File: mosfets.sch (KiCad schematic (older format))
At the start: 28 parts, among them Q11 PSMN1R2-30YLC,115, Q12 PSMN1R2-30YLC,115, Q13 PSMN1R2-30YLC,115, Q14 PMPB20EN, Q15 PMPB20EN, Q16 PMPB20EN, Q17 PMPB20EN

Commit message: Current snapshot
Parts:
- renumbered R41 to R38, R42 to R39, R43 to R40, R44 to R41, R45 to R42, R46 to R43, R47 to R44, R48 to R45, R49 to R46, R50 to R47, R51 to R48, R52 to R49, R53 to R50, R54 to R51
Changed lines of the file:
@@
 $Descr A4 11693 8268
 encoding utf-8
-Sheet 7 7
+Sheet 7 11
 Title "MOSFET"
 Date ""
@@
 Comment4 ""
 $EndDescr
-Text HLabel 2600 1300 2    50   Output ~ 0
-BED_OUT
-Text HLabel 1700 1300 0    50   Output ~ 0
-VDD_BED
 $Comp
 L Device:D_Schottky D22
@@
 PWM_HEAT1
 $Comp
-L Device:R R41
+L Device:R R38
 U 1 1 5B1AEA5D
 P 1500 1750
-F 0 "R41" V 1293 1750 50  0000 C CNN
+F 0 "R38" V 1293 1750 50  0000 C CNN
 F 1 "100" V 1384 1750 50  0000 C CNN
 F 2 "Resistor_SMD:R_0603_1608Metric" V 1430 1750 50  0001 C CNN
@@
 Wire Wire Line
 	2300 1550 2300 1300
-Text HLabel 2600 2950 2    50   Output ~ 0
-HEAT1_OUT
-Text HLabel 1700 2950 0    50   Output ~ 0
-VDD_HEAT1
 $Comp
 L Device:D_Schottky D23
@@
 	2300 3850 2300 3700
 $Comp
-L Device:R R42
+L Device:R R39
 U 1 1 5B1B03DE
 P 1500 3400
-F 0 "R42" V 1293 3400 50  0000 C CNN
+F 0 "R39" V 1293 3400 50  0000 C CNN
 F 1 "100" V 1384 3400 50  0000 C CNN
 F 2 "Resistor_SMD:R_0603_1608Metric" V 1430 3400 50  0001 C CNN
@@
 $EndComp
 $Comp
-L Device:R R47
+L Device:R R44
 U 1 1 5B1FB287
 P 5150 1750
-F 0 "R47" V 4943 1750 50  0000 C CNN
+F 0 "R44" V 4943 1750 50  0000 C CNN
 F 1 "100" V 5034 1750 50  0000 C CNN
 F 2 "Resistor_SMD:R_0603_1608Metric" V 5080 1750 50  0001 C CNN
@@
 Wire Wire Line
 	4900 1750 5000 1750
-Text HLabel 6150 1300 2    50   Output ~ 0
-FAN1_OUT
 Wire Wire Line
 	5250 1300 5350 1300
@@
 	5850 1950 5850 2200
 $Comp
-L Device:R R48
+L Device:R R45
 U 1 1 5B2008D0
 P 5150 3400
-F 0 "R48" V 4943 3400 50  0000 C CNN
+F 0 "R45" V 4943 3400 50  0000 C CNN
 F 1 "100" V 5034 3400 50  0000 C CNN
 F 2 "Resistor_SMD:R_0603_1608Metric" V 5080 3400 50  0001 C CNN
@@
 Wire Wire Line
 	4900 3400 5000 3400
-Text HLabel 6150 2950 2    50   Output ~ 0
-FAN3_OUT
 Wire Wire Line
 	5250 2950 5350 2950
@@
 	1650 3400 1800 3400
 $Comp
-L Device:R R44
+L Device:R R41
 U 1 1 5AF82135
 P 1950 2200
-F 0 "R44" V 1743 2200 50  0000 C CNN
+F 0 "R41" V 1743 2200 50  0000 C CNN
 F 1 "100k" V 1834 2200 50  0000 C CNN
 F 2 "Resistor_SMD:R_0603_1608Metric" V 1880 2200 50  0001 C CNN
@@
 	1800 1750 2000 1750
 $Comp
-L Device:R R45
+L Device:R R42
 U 1 1 5AF8339E
 P 1950 3850
-F 0 "R45" V 1743 3850 50  0000 C CNN
+F 0 "R42" V 1743 3850 50  0000 C CNN
 F 1 "100k" V 1834 3850 50  0000 C CNN
 F 2 "Resistor_SMD:R_0603_1608Metric" V 1880 3850 50  0001 C CNN
@@
 	2300 3850 2100 3850
 $Comp
-L Device:R R49
+L Device:R R46
 U 1 1 5AF83BB4
 P 5600 2200
-F 0 "R49" V 5393 2200 50  0000 C CNN
+F 0 "R46" V 5393 2200 50  0000 C CNN
 F 1 "100k" V 5484 2200 50  0000 C CNN
 F 2 "Resistor_SMD:R_0603_1608Metric" V 5530 2200 50  0001 C CNN
@@
 Connection ~ 5350 1750
 $Comp
-L Device:R R50
+L Device:R R47
 U 1 1 5AF880C0
 P 5650 3850
-F 0 "R50" V 5443 3850 50  0000 C CNN
+F 0 "R47" V 5443 3850 50  0000 C CNN
 F 1 "100k" V 5534 3850 50  0000 C CNN
 F 2 "Resistor_SMD:R_0603_1608Metric" V 5580 3850 50  0001 C CNN
@@
 Text HLabel 1250 4900 0    50   Input ~ 0
 PWM_HEAT2
-Text HLabel 2600 4450 2    50   Output ~ 0
-HEAT2_OUT
-Text HLabel 1700 4450 0    50   Output ~ 0
-VDD_HEAT2
 $Comp
 L Device:D_Schottky D24
@@
 	2300 5350 2300 5200
 $Comp
-L Device:R R43
+L Device:R R40
 U 1 1 5BC4CDF3
 P 1500 4900
-F 0 "R43" V 1293 4900 50  0000 C CNN
+F 0 "R40" V 1293 4900 50  0000 C CNN
 F 1 "100" V 1384 4900 50  0000 C CNN
 F 2 "Resistor_SMD:R_0603_1608Metric" V 1430 4900 50  0001 C CNN
@@
 	1650 4900 1800 4900
 $Comp
-L Device:R R46
+L Device:R R43
 U 1 1 5BC4CE00
 P 1950 5350
-F 0 "R46" V 1743 5350 50  0000 C CNN
+F 0 "R43" V 1743 5350 50  0000 C CNN
 F 1 "100k" V 1834 5350 50  0000 C CNN
 F 2 "Resistor_SMD:R_0603_1608Metric" V 1880 5350 50  0001 C CNN
@@
 Connection ~ 2300 5350
 $Comp
-L power:GND #PWR072
+L power:GND #PWR073
 U 1 1 5BC4EE15
 P 2300 2200
-F 0 "#PWR072" H 2300 1950 50  0001 C CNN
+F 0 "#PWR073" H 2300 1950 50  0001 C CNN
 F 1 "GND" H 2305 2027 50  0000 C CNN
 F 2 "" H 2300 2200 50  0001 C CNN
@@
 $EndComp
 $Comp
-L power:GND #PWR073
+L power:GND #PWR074
 U 1 1 5BC4EE68
 P 2300 3850
-F 0 "#PWR073" H 2300 3600 50  0001 C CNN
+F 0 "#PWR074" H 2300 3600 50  0001 C CNN
 F 1 "GND" H 2305 3677 50  0000 C CNN
 F 2 "" H 2300 3850 50  0001 C CNN
@@
 $EndComp
 $Comp
-L power:GND #PWR074
+L power:GND #PWR075
 U 1 1 5BC50D60
 P 2300 5350
-F 0 "#PWR074" H 2300 5100 50  0001 C CNN
+F 0 "#PWR075" H 2300 5100 50  0001 C CNN
 F 1 "GND" H 2305 5177 50  0000 C CNN
 F 2 "" H 2300 5350 50  0001 C CNN
@@
 $EndComp
 $Comp
-L power:GND #PWR076
+L power:GND #PWR077
 U 1 1 5BC52C58
 P 5850 3850
-F 0 "#PWR076" H 5850 3600 50  0001 C CNN
+F 0 "#PWR077" H 5850 3600 50  0001 C CNN
 F 1 "GND" H 5855 3677 50  0000 C CNN
 F 2 "" H 5850 3850 50  0001 C CNN
@@
 $EndComp
 $Comp
-L power:GND #PWR075
+L power:GND #PWR076
 U 1 1 5BC54B50
 P 5850 2200
-F 0 "#PWR075" H 5850 1950 50  0001 C CNN
+F 0 "#PWR076" H 5850 1950 50  0001 C CNN
 F 1 "GND" H 5855 2027 50  0000 C CNN
 F 2 "" H 5850 2200 50  0001 C CNN
@@
 $EndComp
 $Comp
-L Device:R R51
+L Device:R R48
 U 1 1 5BC57CD1
 P 7600 1750
-F 0 "R51" V 7393 1750 50  0000 C CNN
+F 0 "R48" V 7393 1750 50  0000 C CNN
 F 1 "100" V 7484 1750 50  0000 C CNN
 F 2 "Resistor_SMD:R_0603_1608Metric" V 7530 1750 50  0001 C CNN
@@
 Wire Wire Line
 	7350 1750 7450 1750
-Text HLabel 8600 1300 2    50   Output ~ 0
-FAN2_OUT
 Wire Wire Line
 	7700 1300 7800 1300
@@
 	8300 1950 8300 2200
 $Comp
-L Device:R R52
+L Device:R R49
 U 1 1 5BC57CE1
 P 7600 3400
-F 0 "R52" V 7393 3400 50  0000 C CNN
+F 0 "R49" V 7393 3400 50  0000 C CNN
 F 1 "100" V 7484 3400 50  0000 C CNN
 F 2 "Resistor_SMD:R_0603_1608Metric" V 7530 3400 50  0001 C CNN
@@
 Wire Wire Line
 	7350 3400 7450 3400
-Text HLabel 8600 2950 2    50   Output ~ 0
-FAN4_OUT
 Wire Wire Line
 	7700 2950 7800 2950
@@
 	7800 1750 8000 1750
 $Comp
-L Device:R R53
+L Device:R R50
 U 1 1 5BC57CF2
 P 8050 2200
-F 0 "R53" V 7843 2200 50  0000 C CNN
+F 0 "R50" V 7843 2200 50  0000 C CNN
 F 1 "100k" V 7934 2200 50  0000 C CNN
 F 2 "Resistor_SMD:R_0603_1608Metric" V 7980 2200 50  0001 C CNN
@@
 Connection ~ 7800 1750
 $Comp
-L Device:R R54
+L Device:R R51
 U 1 1 5BC57CFF
 P 8100 3850
-F 0 "R54" V 7893 3850 50  0000 C CNN
+F 0 "R51" V 7893 3850 50  0000 C CNN
 F 1 "100k" V 7984 3850 50  0000 C CNN
 F 2 "Resistor_SMD:R_0603_1608Metric" V 8030 3850 50  0001 C CNN
@@
 	8500 1450 8600 1450
 $Comp
-L power:GND #PWR078
+L power:GND #PWR079
 U 1 1 5BC57D42
 P 8300 3850
-F 0 "#PWR078" H 8300 3600 50  0001 C CNN
+F 0 "#PWR079" H 8300 3600 50  0001 C CNN
 F 1 "GND" H 8305 3677 50  0000 C CNN
 F 2 "" H 8300 3850 50  0001 C CNN
@@
 $EndComp
 $Comp
-L power:GND #PWR077
+L power:GND #PWR078
 U 1 1 5BC57D48
 P 8300 2200
-F 0 "#PWR077" H 8300 1950 50  0001 C CNN
+F 0 "#PWR078" H 8300 1950 50  0001 C CNN
 F 1 "GND" H 8305 2027 50  0000 C CNN
 F 2 "" H 8300 2200 50  0001 C CNN
@@
 	1    0    0    -1
 $EndComp
+Text GLabel 1700 1300 0    50   Input ~ 0
+VDD_BED
+Text GLabel 1700 2950 0    50   Input ~ 0
+VDD_HEAT1
+Text GLabel 1700 4450 0    50   Input ~ 0
+VDD_HEAT2
+Text GLabel 2600 1300 2    50   Input ~ 0
+BED_OUT
+Text GLabel 2600 2950 2    50   Input ~ 0
+HEAT1_OUT
+Text GLabel 2600 4450 2    50   Input ~ 0
+HEAT2_OUT
+Text GLabel 6150 1300 2    50   Input ~ 0
+FAN1_OUT
+Text GLabel 8600 1300 2    50   Input ~ 0
+FAN2_OUT
+Text GLabel 6150 2950 2    50   Input ~ 0
+FAN3_OUT
+Text GLabel 8600 2950 2    50   Input ~ 0
+FAN4_OUT
 $EndSCHEMATC

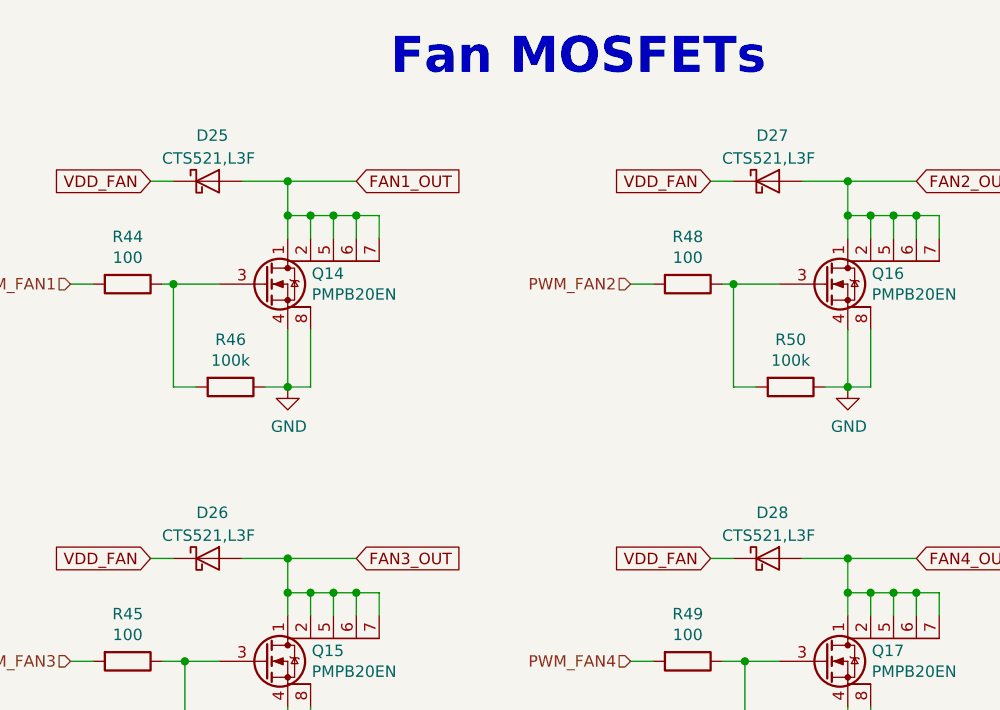
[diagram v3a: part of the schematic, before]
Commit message: Various changes
* Add Status LED
* Switched small diodes to more general available BAT54 in SOD123
* Fixed various DRC errors
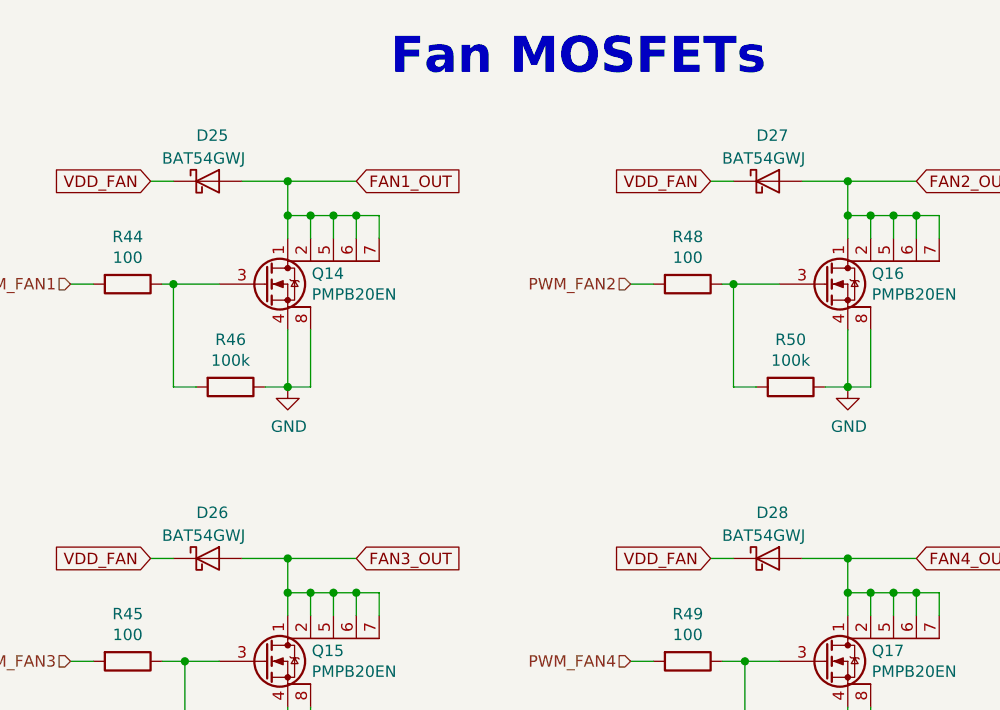
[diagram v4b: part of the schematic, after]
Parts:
- D25, D26, D27, D28: value CTS521,L3F -> BAT54GWJ; footprint heteromycin:SOD882 -> Diode_SMD:D_SOD-123
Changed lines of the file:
@@
 P 5500 1300
 F 0 "D25" H 5450 1500 50  0000 L CNN
-F 1 "CTS521,L3F" H 5300 1400 50  0000 L CNN
-F 2 "heteromycin:SOD882" H 5500 1300 50  0001 C CNN
-F 3 "http://toshiba.semicon-storage.com/info/lookup.jsp?pid=CTS521&lang=en" H 5500 1300 50  0001 C CNN
+F 1 "BAT54GWJ" H 5300 1400 50  0000 L CNN
+F 2 "Diode_SMD:D_SOD-123" H 5500 1300 50  0001 C CNN
+F 3 "https://www.mouser.de/datasheet/2/916/BAT54GW-1318921.pdf" H 5500 1300 50  0001 C CNN
 	1    5500 1300
 	1    0    0    -1
@@
 P 5500 2950
 F 0 "D26" H 5450 3150 50  0000 L CNN
-F 1 "CTS521,L3F" H 5300 3050 50  0000 L CNN
-F 2 "heteromycin:SOD882" H 5500 2950 50  0001 C CNN
-F 3 "http://toshiba.semicon-storage.com/info/lookup.jsp?pid=CTS521&lang=en" H 5500 2950 50  0001 C CNN
+F 1 "BAT54GWJ" H 5300 3050 50  0000 L CNN
+F 2 "Diode_SMD:D_SOD-123" H 5500 2950 50  0001 C CNN
+F 3 "https://www.mouser.de/datasheet/2/916/BAT54GW-1318921.pdf" H 5500 2950 50  0001 C CNN
 	1    5500 2950
 	1    0    0    -1
@@
 P 7950 1300
 F 0 "D27" H 7900 1500 50  0000 L CNN
-F 1 "CTS521,L3F" H 7750 1400 50  0000 L CNN
-F 2 "heteromycin:SOD882" H 7950 1300 50  0001 C CNN
-F 3 "http://toshiba.semicon-storage.com/info/lookup.jsp?pid=CTS521&lang=en" H 7950 1300 50  0001 C CNN
+F 1 "BAT54GWJ" H 7750 1400 50  0000 L CNN
+F 2 "Diode_SMD:D_SOD-123" H 7950 1300 50  0001 C CNN
+F 3 "https://www.mouser.de/datasheet/2/916/BAT54GW-1318921.pdf" H 7950 1300 50  0001 C CNN
 	1    7950 1300
 	1    0    0    -1
@@
 P 7950 2950
 F 0 "D28" H 7900 3150 50  0000 L CNN
-F 1 "CTS521,L3F" H 7750 3050 50  0000 L CNN
-F 2 "heteromycin:SOD882" H 7950 2950 50  0001 C CNN
-F 3 "http://toshiba.semicon-storage.com/info/lookup.jsp?pid=CTS521&lang=en" H 7950 2950 50  0001 C CNN
+F 1 "BAT54GWJ" H 7750 3050 50  0000 L CNN
+F 2 "Diode_SMD:D_SOD-123" H 7950 2950 50  0001 C CNN
+F 3 "https://www.mouser.de/datasheet/2/916/BAT54GW-1318921.pdf" H 7950 2950 50  0001 C CNN
 	1    7950 2950
 	1    0    0    -1

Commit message: Complete functional design
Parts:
- renumbered D24 to D10, D25 to D11, D26 to D12, D27 to D13, D28 to D14, D22 to D8, D23 to D9, R38 to R30, R39 to R31, R40 to R32, R41 to R33, R42 to R34, R43 to R35, R44 to R36, R45 to R37, R46 to R38, R47 to R39, R48 to R40, R49 to R41, R50 to R42, R51 to R43
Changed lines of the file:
@@
 $EndDescr
 $Comp
-L Device:D_Schottky D22
+L Device:D_Schottky D8
 U 1 1 5B1A3271
 P 1950 1300
-F 0 "D22" H 1950 1516 50  0000 C CNN
+F 0 "D8" H 1950 1516 50  0000 C CNN
 F 1 "SK310A-LTP" H 1950 1425 50  0000 C CNN
 F 2 "Diode_SMD:D_SMA" H 1950 1300 50  0001 C CNN
@@
 PWM_HEAT1
 $Comp
-L Device:R R38
+L Device:R R30
 U 1 1 5B1AEA5D
 P 1500 1750
-F 0 "R38" V 1293 1750 50  0000 C CNN
+F 0 "R30" V 1293 1750 50  0000 C CNN
 F 1 "100" V 1384 1750 50  0000 C CNN
 F 2 "Resistor_SMD:R_0603_1608Metric" V 1430 1750 50  0001 C CNN
@@
 	2300 1550 2300 1300
 $Comp
-L Device:D_Schottky D23
+L Device:D_Schottky D9
 U 1 1 5B1B03B6
 P 1950 2950
-F 0 "D23" H 1950 3166 50  0000 C CNN
+F 0 "D9" H 1950 3166 50  0000 C CNN
 F 1 "SK310A-LTP" H 1950 3075 50  0000 C CNN
 F 2 "Diode_SMD:D_SMA" H 1950 2950 50  0001 C CNN
@@
 	2300 3850 2300 3700
 $Comp
-L Device:R R39
+L Device:R R31
 U 1 1 5B1B03DE
 P 1500 3400
-F 0 "R39" V 1293 3400 50  0000 C CNN
+F 0 "R31" V 1293 3400 50  0000 C CNN
 F 1 "100" V 1384 3400 50  0000 C CNN
 F 2 "Resistor_SMD:R_0603_1608Metric" V 1430 3400 50  0001 C CNN
@@
 $EndComp
 $Comp
-L Device:R R44
+L Device:R R36
 U 1 1 5B1FB287
 P 5150 1750
-F 0 "R44" V 4943 1750 50  0000 C CNN
+F 0 "R36" V 4943 1750 50  0000 C CNN
 F 1 "100" V 5034 1750 50  0000 C CNN
 F 2 "Resistor_SMD:R_0603_1608Metric" V 5080 1750 50  0001 C CNN
@@
 	5850 1950 5850 2200
 $Comp
-L Device:R R45
+L Device:R R37
 U 1 1 5B2008D0
 P 5150 3400
-F 0 "R45" V 4943 3400 50  0000 C CNN
+F 0 "R37" V 4943 3400 50  0000 C CNN
 F 1 "100" V 5034 3400 50  0000 C CNN
 F 2 "Resistor_SMD:R_0603_1608Metric" V 5080 3400 50  0001 C CNN
@@
 	1650 3400 1800 3400
 $Comp
-L Device:R R41
+L Device:R R33
 U 1 1 5AF82135
 P 1950 2200
-F 0 "R41" V 1743 2200 50  0000 C CNN
+F 0 "R33" V 1743 2200 50  0000 C CNN
 F 1 "100k" V 1834 2200 50  0000 C CNN
 F 2 "Resistor_SMD:R_0603_1608Metric" V 1880 2200 50  0001 C CNN
@@
 	1800 1750 2000 1750
 $Comp
-L Device:R R42
+L Device:R R34
 U 1 1 5AF8339E
 P 1950 3850
-F 0 "R42" V 1743 3850 50  0000 C CNN
+F 0 "R34" V 1743 3850 50  0000 C CNN
 F 1 "100k" V 1834 3850 50  0000 C CNN
 F 2 "Resistor_SMD:R_0603_1608Metric" V 1880 3850 50  0001 C CNN
@@
 	2300 3850 2100 3850
 $Comp
-L Device:R R46
+L Device:R R38
 U 1 1 5AF83BB4
 P 5600 2200
-F 0 "R46" V 5393 2200 50  0000 C CNN
+F 0 "R38" V 5393 2200 50  0000 C CNN
 F 1 "100k" V 5484 2200 50  0000 C CNN
 F 2 "Resistor_SMD:R_0603_1608Metric" V 5530 2200 50  0001 C CNN
@@
 Connection ~ 5350 1750
 $Comp
-L Device:R R47
+L Device:R R39
 U 1 1 5AF880C0
 P 5650 3850
-F 0 "R47" V 5443 3850 50  0000 C CNN
+F 0 "R39" V 5443 3850 50  0000 C CNN
 F 1 "100k" V 5534 3850 50  0000 C CNN
 F 2 "Resistor_SMD:R_0603_1608Metric" V 5580 3850 50  0001 C CNN
@@
 $EndComp
 $Comp
-L Device:D_Schottky D25
+L Device:D_Schottky D11
 U 1 1 5BD6B250
 P 5500 1300
-F 0 "D25" H 5450 1500 50  0000 L CNN
+F 0 "D11" H 5450 1500 50  0000 L CNN
 F 1 "BAT54GWJ" H 5300 1400 50  0000 L CNN
 F 2 "Diode_SMD:D_SOD-123" H 5500 1300 50  0001 C CNN
@@
 $EndComp
 $Comp
-L Device:D_Schottky D26
+L Device:D_Schottky D12
 U 1 1 5BD6D4A2
 P 5500 2950
-F 0 "D26" H 5450 3150 50  0000 L CNN
+F 0 "D12" H 5450 3150 50  0000 L CNN
 F 1 "BAT54GWJ" H 5300 3050 50  0000 L CNN
 F 2 "Diode_SMD:D_SOD-123" H 5500 2950 50  0001 C CNN
@@
 PWM_HEAT2
 $Comp
-L Device:D_Schottky D24
+L Device:D_Schottky D10
 U 1 1 5BC4CDE5
 P 1950 4450
-F 0 "D24" H 1950 4666 50  0000 C CNN
+F 0 "D10" H 1950 4666 50  0000 C CNN
 F 1 "SK310A-LTP" H 1950 4575 50  0000 C CNN
 F 2 "Diode_SMD:D_SMA" H 1950 4450 50  0001 C CNN
@@
 	2300 5350 2300 5200
 $Comp
-L Device:R R40
+L Device:R R32
 U 1 1 5BC4CDF3
 P 1500 4900
-F 0 "R40" V 1293 4900 50  0000 C CNN
+F 0 "R32" V 1293 4900 50  0000 C CNN
 F 1 "100" V 1384 4900 50  0000 C CNN
 F 2 "Resistor_SMD:R_0603_1608Metric" V 1430 4900 50  0001 C CNN
@@
 	1650 4900 1800 4900
 $Comp
-L Device:R R43
+L Device:R R35
 U 1 1 5BC4CE00
 P 1950 5350
-F 0 "R43" V 1743 5350 50  0000 C CNN
+F 0 "R35" V 1743 5350 50  0000 C CNN
 F 1 "100k" V 1834 5350 50  0000 C CNN
 F 2 "Resistor_SMD:R_0603_1608Metric" V 1880 5350 50  0001 C CNN
@@
 Connection ~ 2300 5350
 $Comp
-L power:GND #PWR073
+L power:GND #PWR057
 U 1 1 5BC4EE15
 P 2300 2200
-F 0 "#PWR073" H 2300 1950 50  0001 C CNN
+F 0 "#PWR057" H 2300 1950 50  0001 C CNN
 F 1 "GND" H 2305 2027 50  0000 C CNN
 F 2 "" H 2300 2200 50  0001 C CNN
@@
 $EndComp
 $Comp
-L power:GND #PWR074
+L power:GND #PWR058
 U 1 1 5BC4EE68
 P 2300 3850
-F 0 "#PWR074" H 2300 3600 50  0001 C CNN
+F 0 "#PWR058" H 2300 3600 50  0001 C CNN
 F 1 "GND" H 2305 3677 50  0000 C CNN
 F 2 "" H 2300 3850 50  0001 C CNN
@@
 $EndComp
 $Comp
-L power:GND #PWR075
+L power:GND #PWR059
 U 1 1 5BC50D60
 P 2300 5350
-F 0 "#PWR075" H 2300 5100 50  0001 C CNN
+F 0 "#PWR059" H 2300 5100 50  0001 C CNN
 F 1 "GND" H 2305 5177 50  0000 C CNN
 F 2 "" H 2300 5350 50  0001 C CNN
@@
 $EndComp
 $Comp
-L power:GND #PWR077
+L power:GND #PWR061
 U 1 1 5BC52C58
 P 5850 3850
-F 0 "#PWR077" H 5850 3600 50  0001 C CNN
+F 0 "#PWR061" H 5850 3600 50  0001 C CNN
 F 1 "GND" H 5855 3677 50  0000 C CNN
 F 2 "" H 5850 3850 50  0001 C CNN
@@
 $EndComp
 $Comp
-L power:GND #PWR076
+L power:GND #PWR060
 U 1 1 5BC54B50
 P 5850 2200
-F 0 "#PWR076" H 5850 1950 50  0001 C CNN
+F 0 "#PWR060" H 5850 1950 50  0001 C CNN
 F 1 "GND" H 5855 2027 50  0000 C CNN
 F 2 "" H 5850 2200 50  0001 C CNN
@@
 $EndComp
 $Comp
-L Device:R R48
+L Device:R R40
 U 1 1 5BC57CD1
 P 7600 1750
-F 0 "R48" V 7393 1750 50  0000 C CNN
+F 0 "R40" V 7393 1750 50  0000 C CNN
 F 1 "100" V 7484 1750 50  0000 C CNN
 F 2 "Resistor_SMD:R_0603_1608Metric" V 7530 1750 50  0001 C CNN
@@
 	8300 1950 8300 2200
 $Comp
-L Device:R R49
+L Device:R R41
 U 1 1 5BC57CE1
 P 7600 3400
-F 0 "R49" V 7393 3400 50  0000 C CNN
+F 0 "R41" V 7393 3400 50  0000 C CNN
 F 1 "100" V 7484 3400 50  0000 C CNN
 F 2 "Resistor_SMD:R_0603_1608Metric" V 7530 3400 50  0001 C CNN
@@
 	7800 1750 8000 1750
 $Comp
-L Device:R R50
+L Device:R R42
 U 1 1 5BC57CF2
 P 8050 2200
-F 0 "R50" V 7843 2200 50  0000 C CNN
+F 0 "R42" V 7843 2200 50  0000 C CNN
 F 1 "100k" V 7934 2200 50  0000 C CNN
 F 2 "Resistor_SMD:R_0603_1608Metric" V 7980 2200 50  0001 C CNN
@@
 Connection ~ 7800 1750
 $Comp
-L Device:R R51
+L Device:R R43
 U 1 1 5BC57CFF
 P 8100 3850
-F 0 "R51" V 7893 3850 50  0000 C CNN
+F 0 "R43" V 7893 3850 50  0000 C CNN
 F 1 "100k" V 7984 3850 50  0000 C CNN
 F 2 "Resistor_SMD:R_0603_1608Metric" V 8030 3850 50  0001 C CNN
@@
 VDD_FAN
 $Comp
-L Device:D_Schottky D27
+L Device:D_Schottky D13
 U 1 1 5BC57D0F
 P 7950 1300
-F 0 "D27" H 7900 1500 50  0000 L CNN
+F 0 "D13" H 7900 1500 50  0000 L CNN
 F 1 "BAT54GWJ" H 7750 1400 50  0000 L CNN
 F 2 "Diode_SMD:D_SOD-123" H 7950 1300 50  0001 C CNN
@@
 $EndComp
 $Comp
-L Device:D_Schottky D28
+L Device:D_Schottky D14
 U 1 1 5BC57D16
 P 7950 2950
-F 0 "D28" H 7900 3150 50  0000 L CNN
+F 0 "D14" H 7900 3150 50  0000 L CNN
 F 1 "BAT54GWJ" H 7750 3050 50  0000 L CNN
 F 2 "Diode_SMD:D_SOD-123" H 7950 2950 50  0001 C CNN
@@
 	8500 1450 8600 1450
 $Comp
-L power:GND #PWR079
+L power:GND #PWR063
 U 1 1 5BC57D42
 P 8300 3850
-F 0 "#PWR079" H 8300 3600 50  0001 C CNN
+F 0 "#PWR063" H 8300 3600 50  0001 C CNN
 F 1 "GND" H 8305 3677 50  0000 C CNN
 F 2 "" H 8300 3850 50  0001 C CNN
@@
 $EndComp
 $Comp
-L power:GND #PWR078
+L power:GND #PWR062
 U 1 1 5BC57D48
 P 8300 2200
-F 0 "#PWR078" H 8300 1950 50  0001 C CNN
+F 0 "#PWR062" H 8300 1950 50  0001 C CNN
 F 1 "GND" H 8305 2027 50  0000 C CNN
 F 2 "" H 8300 2200 50  0001 C CNN
